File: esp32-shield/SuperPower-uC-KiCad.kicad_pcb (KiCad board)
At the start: 2 copper layers, 45.1 x 45.1 mm, 34 parts, among them J11 DNP, J5 Conn_01x14_Female, J6 Conn_01x14_Female, J9 MCU board, Q3 S8050, Q4 S8050, SW1 SKRKAEE020, U13 ESP32-WROOM32, U14 W25Q32JVSS, U4 SN74LV1T34DBV, U5 CH340C, U6 AMS1117-3.3

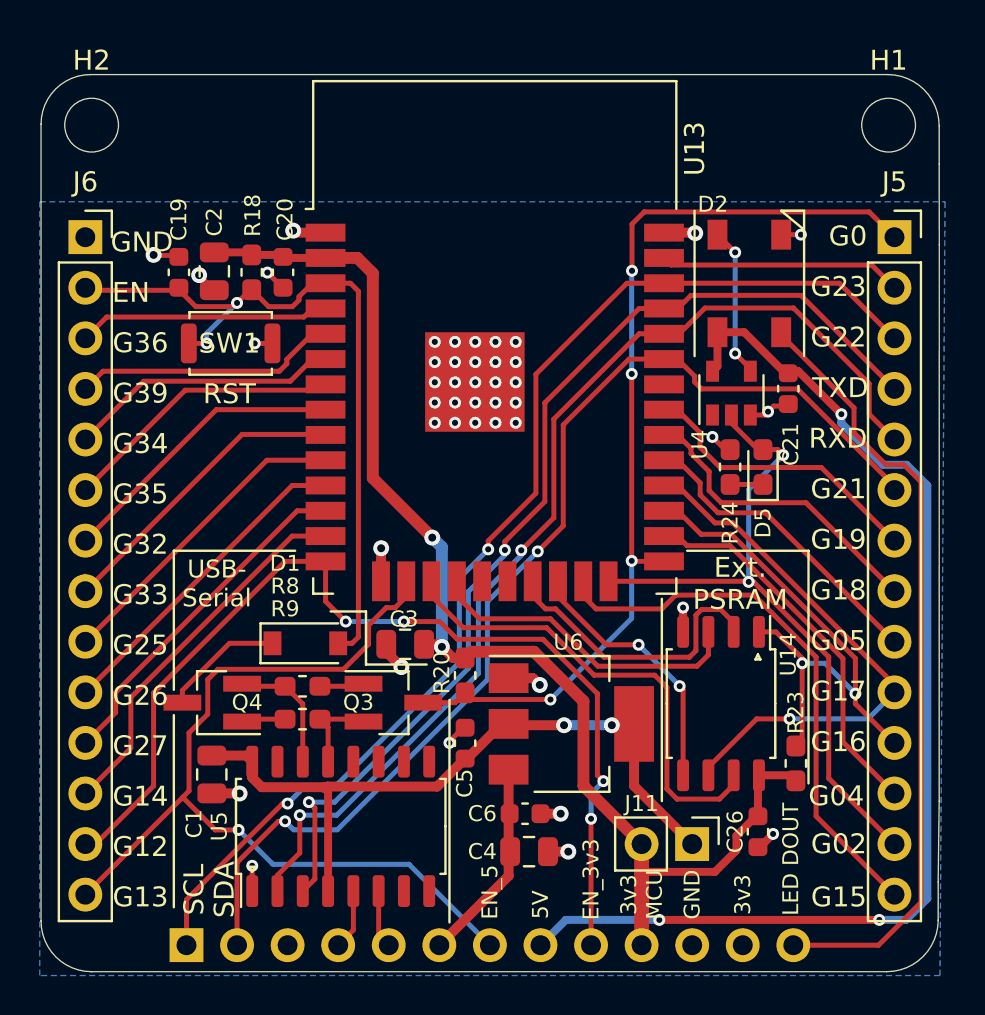
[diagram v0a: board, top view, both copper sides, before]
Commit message: swapped jumper with solderbridge
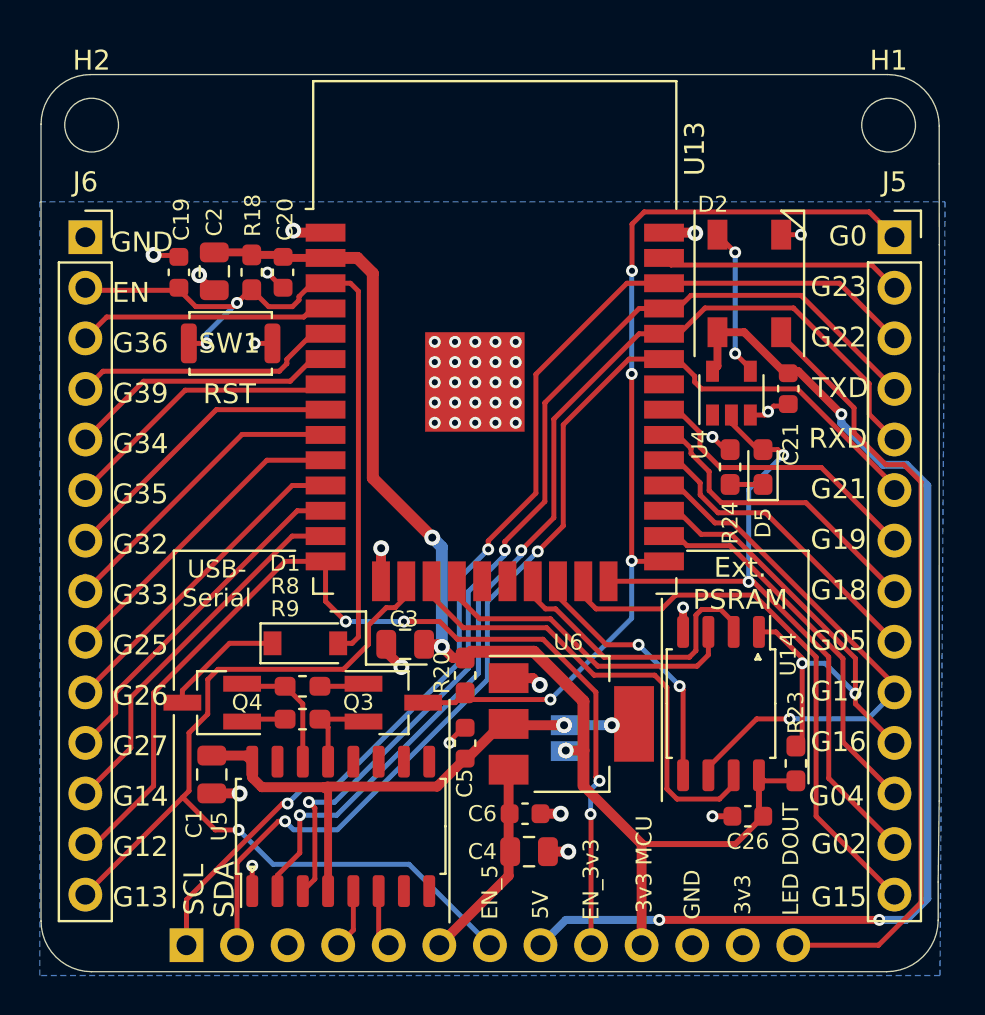
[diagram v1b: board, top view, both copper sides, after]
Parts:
- removed J11: DNP, Connector_PinHeader_2.54mm:PinHeader_1x02_P2.54mm_Vertical
- added JP1: Jumper_2_Open, Jumper:SolderJumper-2_P1.3mm_Open_Pad1.0x1.5mm, B.Cu at (152.2, 106.7)
- moved C26 0.93 mm to (161.4, 110.6), turned to 0 degrees
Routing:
- net /MCU Module/3v3_UART: track 36.5 -> 29.3 mm
- net /3v3_MCU: track 63.0 -> 63.3 mm, vias 2 -> 3

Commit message: fixed silk positioning
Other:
- board text added: "v1.1 (2021-08)"
- board text removed: "v1.1 (2021-05)"

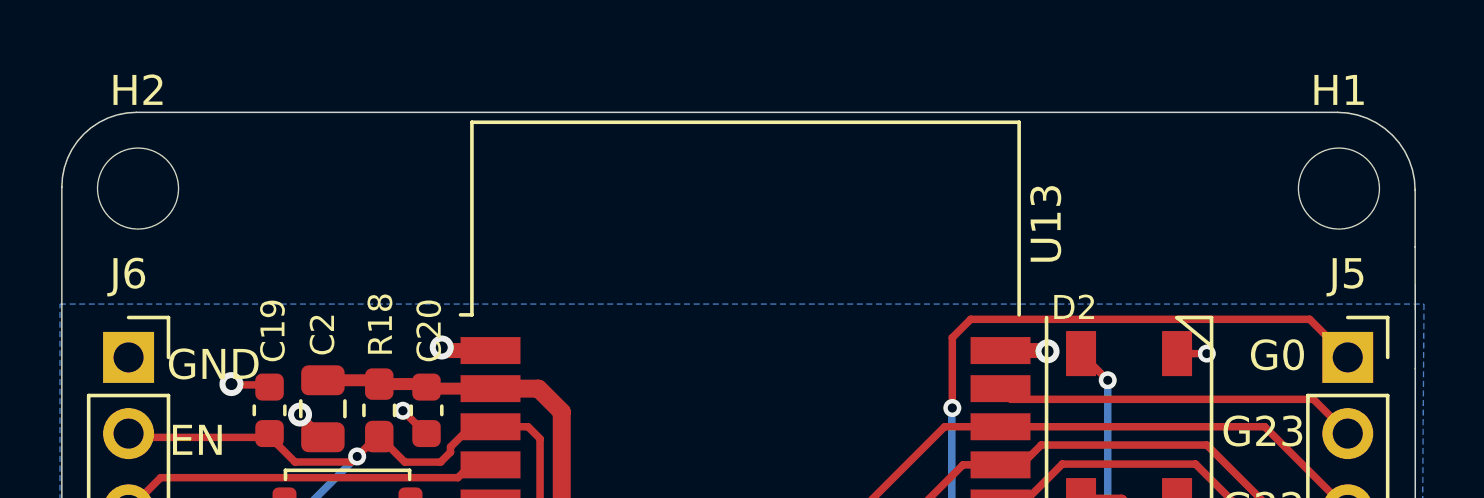
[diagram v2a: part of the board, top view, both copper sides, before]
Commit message: Marked components DNP
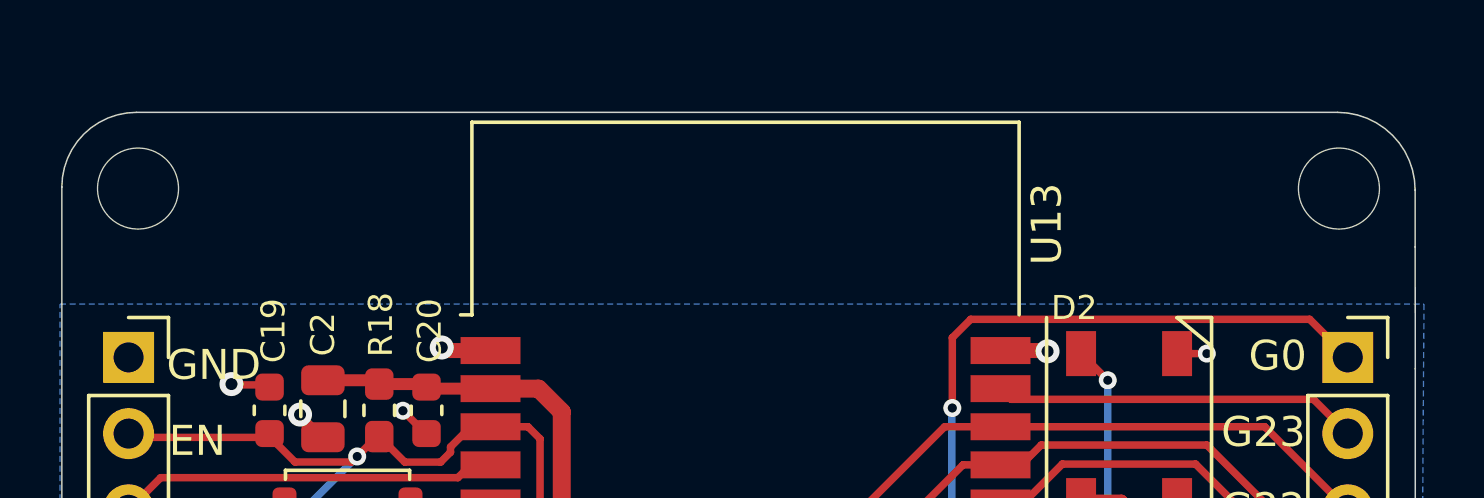
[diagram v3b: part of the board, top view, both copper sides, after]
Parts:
- C26: value 1µF -> DNP/1µF
- J5, J6: value Conn_01x14_Female -> DNP/Conn_01x14_Female
- R23: value 10k -> DNP/10k
- U14: value W25Q32JVSS -> DNP/W25Q32JVSS
